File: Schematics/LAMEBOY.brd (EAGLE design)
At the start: 45.7 x 67.3 mm, 60 parts, among them IC1 PCF8574T, IC3 MCP73831, Q1 12MHz, U1 USD-SOCKETMICROSDEBAY, U2 USB

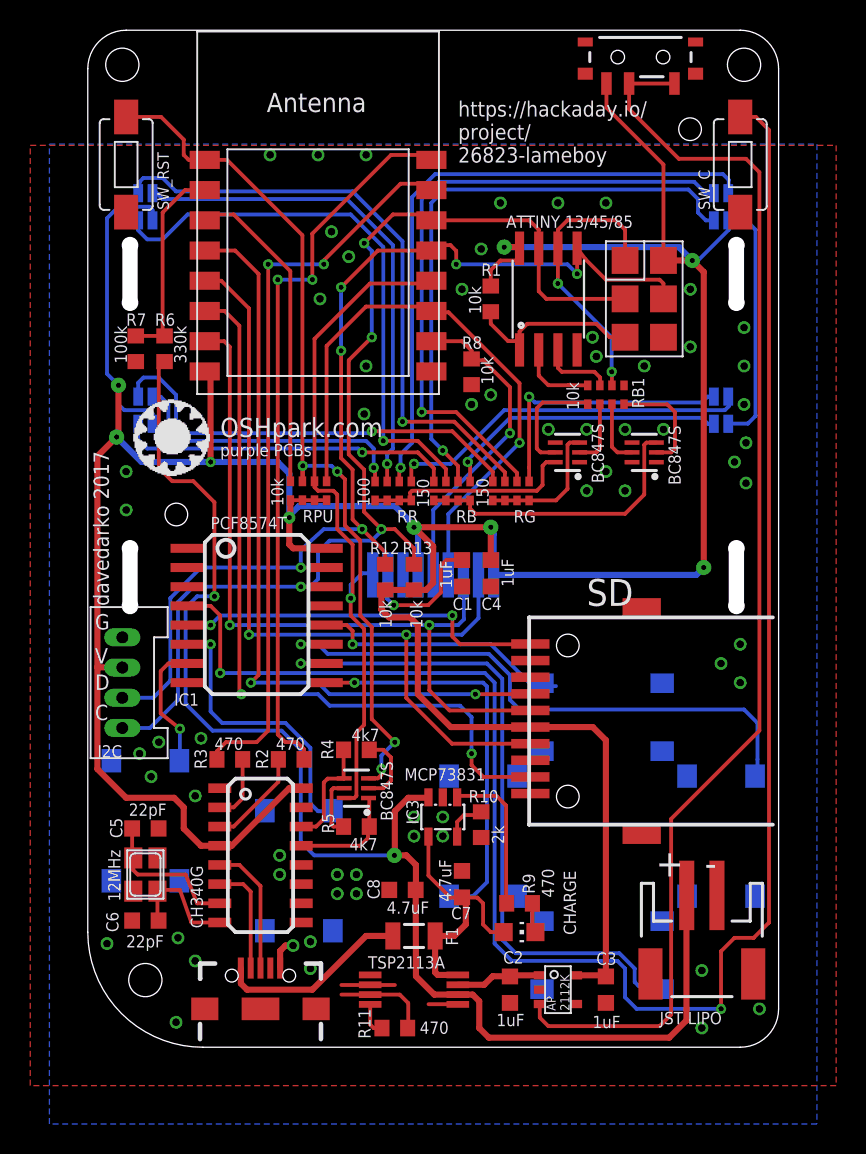
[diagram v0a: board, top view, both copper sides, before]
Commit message: bigger better resistor and crystal footprint
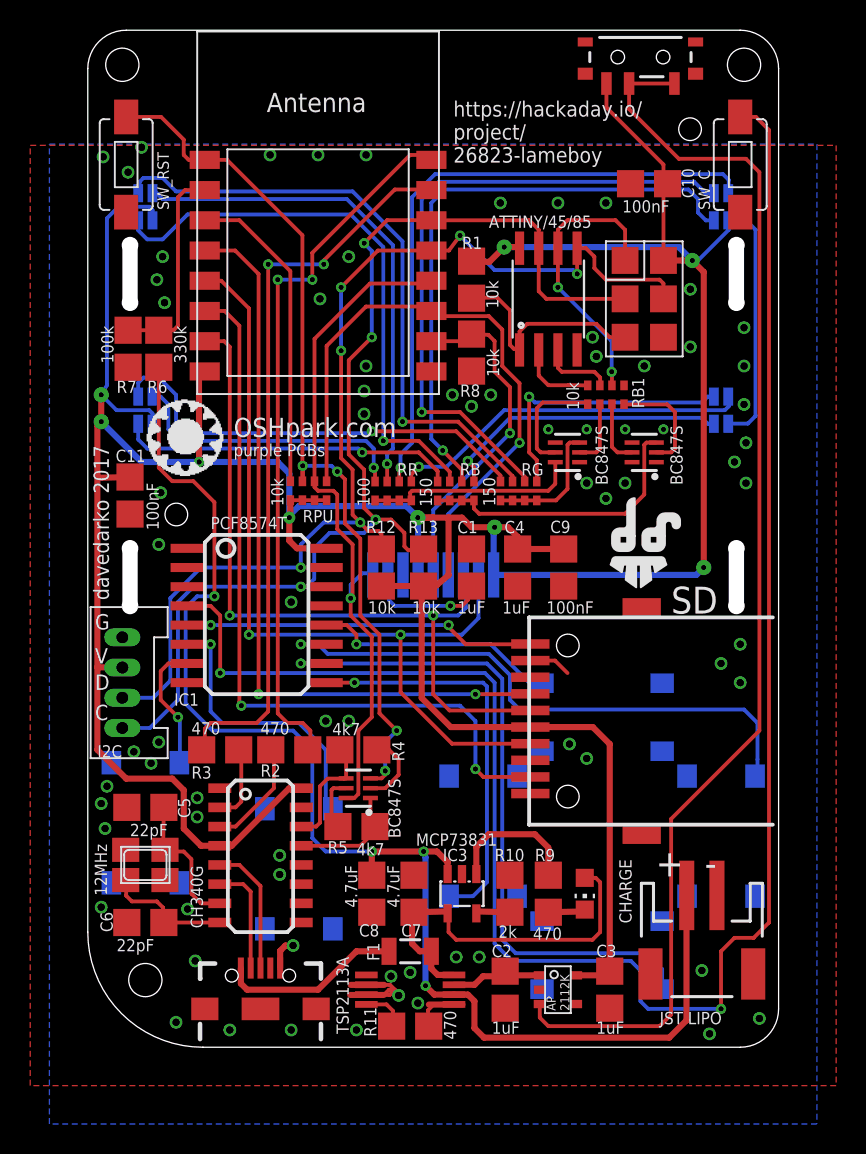
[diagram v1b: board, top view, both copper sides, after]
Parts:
- added C10, C11, C9: 100nF, rcl:ONEFITSALL
- added U$11: (no value), LOGOS:DAVEDARKO2_LOGO
- C1, C2, C3, C4, C5, C6, C7, C8: device rcl:C0603K -> rcl:ONEFITSALL
- Q1: device adafruit:NX3225 -> adafruit:NX3225_BIGGER
- R1, R10, R11, R12, R13, R2, R3, R4, R5, R6, R7, R8, R9: device rcl:R0603 -> rcl:ONEFITSALL
- U$8: device LOGOS:HACKADAY_LOGO -> LOGOS:DAVEDARKO_GOLD
- moved IC3 5.24 mm to (24.8, 10.2)
- moved CHARGE 5.01 mm to (32.9, 10.2), turned to 180 degrees
- moved R10 4.95 mm to (27.9, 10.2), turned to 270 degrees
- moved C7 3.24 mm to (21.6, 10.2)
- moved C8 2.05 mm to (18.8, 10.2), turned to 270 degrees
- moved R9 2.01 mm to (30.5, 10.2), turned to 90 degrees
- moved C4 1.82 mm to (28.4, 31.8)
- moved R1 1.80 mm to (25.4, 50.8)
- moved C5 1.40 mm to (3.81, 15.9), turned to 0 degrees
- moved R8 1.27 mm to (25.4, 46.0)
- moved U$8 1.05 mm to (34.0, 12.7), turned to 0 degrees
- moved F1 1.05 mm to (21.3, 6.35)
- moved R11 1.02 mm to (21.3, 1.40)
- moved R13 0.90 mm to (22.2, 31.8)
- moved R3 0.90 mm to (8.76, 19.7)
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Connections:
- net VREG_OUT renamed VREG_EN
- net ADC: now also R6.P$1, R7.P$2; no longer R6.1, R7.2
- net AVR_RST: now also R1.P$1; no longer R1.1
- net DTR: now also R5.P$1; no longer R5.1
- net GND: now also C1.P$2, C10.P$1, C11.P$1, C2.P$2, C3.P$2, C4.P$2, C5.P$1, C6.P$1, C7.P$1, C8.P$2, C9.P$1, R10.P$1, R11.P$1, R7.P$1, R8.P$2; no longer C1.2, C2.2, C3.2, C4.2, C5.1, C6.1, C7.1, C8.2, R10.1, R11.1, R7.1, R8.2
- net GPIO15: now also R8.P$1; no longer R8.1
- net N$12: now also R9.P$2; no longer R9.2
- net N$15: now also R9.P$1; no longer R9.1
- net N$17: now also C5.P$2; no longer C5.2
- net N$20: now also R11.P$2; no longer R11.2
- net N$21: now also R10.P$2; no longer R10.2
- net N$24: now also C6.P$2; no longer C6.2
- net N$25: now also R5.P$2; no longer R5.2
- net N$26: now also R2.P$2; no longer R2.2
- net N$27: now also R3.P$2; no longer R3.2
- net N$28: now also R4.P$2; no longer R4.2
- net N$8: now also C1.P$1; no longer C1.1
- net RTS: now also R4.P$1; no longer R4.1
- net RX_ESP: now also R3.P$1; no longer R3.1
- net SCL: now also R13.P$2; no longer R13.2
- net SDA: now also R12.P$2; no longer R12.2
- net TX_ESP: now also R2.P$1; no longer R2.1
- net VBAT: now also C8.P$1, R6.P$2; no longer C8.1, R6.2
- net VBUS: now also C7.P$2; no longer C7.2
- net VCC: now also C10.P$2, C11.P$2, C3.P$1, C4.P$1, C9.P$2, R1.P$2, R12.P$1, R13.P$1; no longer C3.1, C4.1, R1.2, R12.1, R13.1
- net VREG_IN: now also C2.P$1; no longer C2.1
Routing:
- net VBUS: track 18.2 -> 24.9 mm
- net VCC: track 254.7 -> 261.0 mm
- net GND: track 14.3 -> 17.8 mm, vias 63 -> 75
- net AVR_RST: track 12.4 -> 14.7 mm
- net BTN_UP: track 17.9 -> 16.3 mm
- net GPIO2: track 39.9 -> 41.3 mm
- net SD_IN: track 24.6 -> 23.3 mm
- net VREG_IN: track 5.70 -> 6.76 mm
- net DTR: track 7.34 -> 8.37 mm
- net GPIO15: track 21.7 -> 22.7 mm
- net TX_ESP: track 48.6 -> 47.6 mm
- net RX_ESP: track 48.9 -> 49.9 mm
- net N$20: track 2.21 -> 3.17 mm
- net N$12: track 10.1 -> 9.11 mm
- net N$21: track 3.13 -> 2.28 mm
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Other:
- board text added: "ATTINY/45/85"
- board text removed: "ATTINY 13/45/85"

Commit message: no idea. there's stuff changed so I push.
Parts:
- added U$12: (no value), LOGOS:HACKADAY_LOGO
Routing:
- net GND: vias 75 -> 76
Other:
- board text added: "*OR THE DISPLAY WON'T FIT"
- board text added: "ORDER 0.8MM BOARDS*"
- board text added: "Put the ESP8266 module here - it has all the WIFI"
- board text added: "This knows all the buttons"
- board text added: "This will come in handy one day. Please help."
- board text added: "USB serial converter"

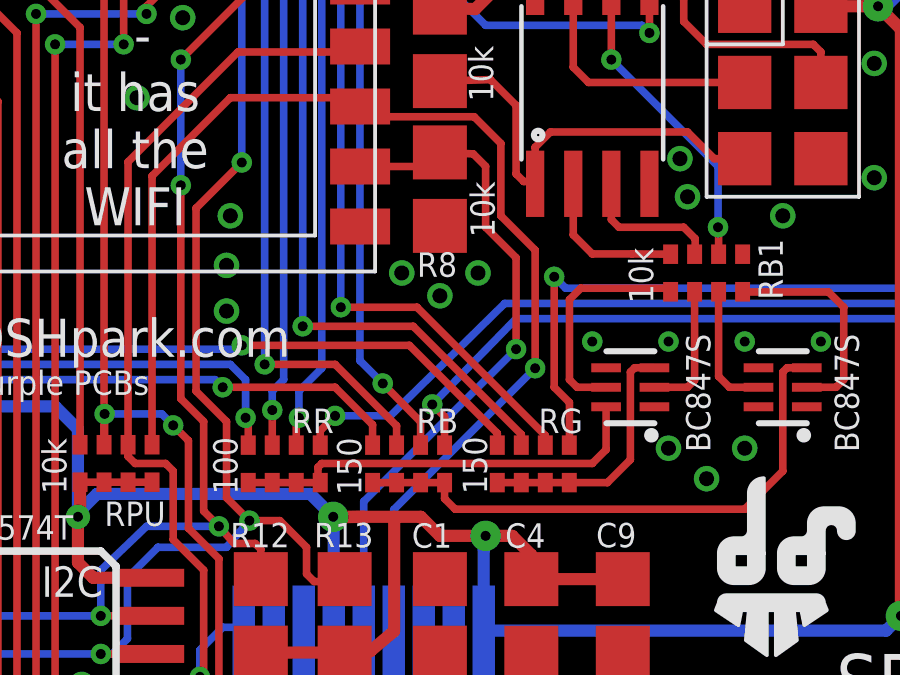
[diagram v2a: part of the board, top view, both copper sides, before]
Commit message: corrected rgb layout
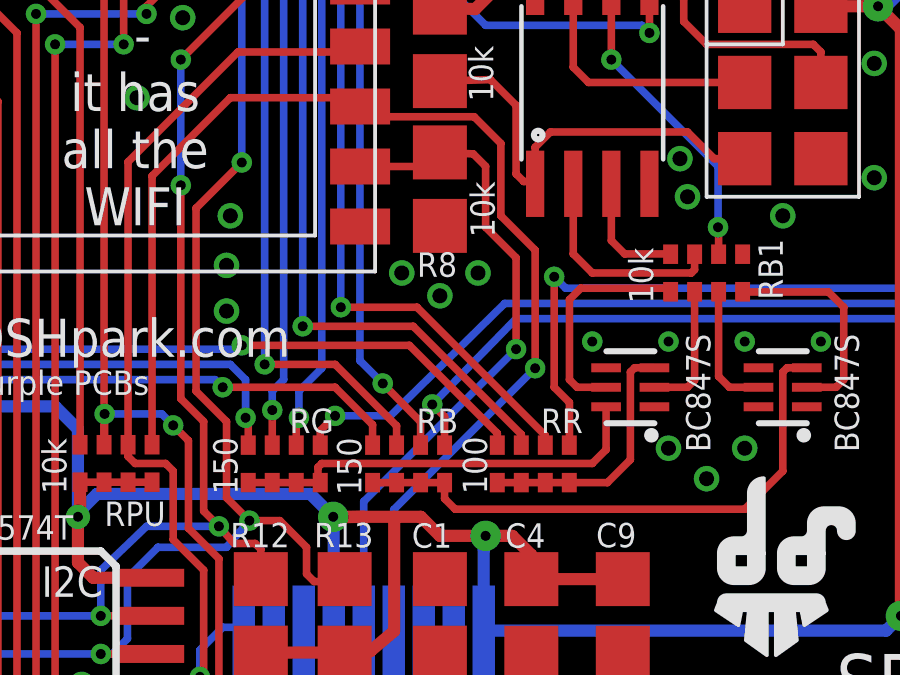
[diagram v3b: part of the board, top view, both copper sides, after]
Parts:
- moved RG 8.30 mm to (20.2, 36.8)
- moved RR 8.30 mm to (28.5, 36.8)
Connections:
- net N$1 renamed BLUE_LED
- removed net N$2: LED4.3, RR.4
- removed net N$3: LED4.2, RG.4
- new net GREEN_LED: LED4.3, RG.4
- new net RED_LED: LED4.2, RR.4
- net C_GRN: now also RB1.7; no longer RB1.8
- net C_RED: now also RB1.8; no longer RB1.7
- net GRN: now also U$6.6; no longer U$6.3
- net L2_R: now also RG.1; no longer RR.1
- net L4_G: now also RR.1; no longer RG.1
- net N$10: now also RR.2; no longer RG.2
- net N$5: now also RG.3; no longer RR.3
- net N$6: now also RR.3; no longer RG.3
- net N$9: now also RG.2; no longer RR.2
- net RED: now also U$6.3; no longer U$6.6
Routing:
- net RED_LED: track 0.00 -> 29.3 mm, vias 0 -> 1
- net N$3: track 29.3 -> 0.00 mm, vias 1 -> 0
- net N$2: track 19.2 -> 0.00 mm, vias 1 -> 0
- net GREEN_LED: track 0.00 -> 19.2 mm, vias 0 -> 1
- net RED: track 14.2 -> 8.53 mm
- net GRN: track 8.53 -> 14.2 mm
- net C_GRN: track 5.21 -> 7.21 mm
- net C_RED: track 4.78 -> 4.06 mm
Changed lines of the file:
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@@
 <layer number="20" name="Dimension" color="15" fill="1" visible="yes" active="yes"/>
 <layer number="21" name="tPlace" color="7" fill="1" visible="yes" active="yes"/>
-<layer number="22" name="bPlace" color="7" fill="1" visible="no" active="yes"/>
+<layer number="22" name="bPlace" color="7" fill="1" visible="yes" active="yes"/>
 <layer number="23" name="tOrigins" color="15" fill="1" visible="yes" active="yes"/>
-<layer number="24" name="bOrigins" color="15" fill="1" visible="no" active="yes"/>
+<layer number="24" name="bOrigins" color="15" fill="1" visible="yes" active="yes"/>
 <layer number="25" name="tNames" color="7" fill="1" visible="yes" active="yes"/>
-<layer number="26" name="bNames" color="7" fill="1" visible="no" active="yes"/>
-<layer number="27" name="tValues" color="7" fill="1" visible="no" active="yes"/>
-<layer number="28" name="bValues" color="7" fill="1" visible="no" active="yes"/>
+<layer number="26" name="bNames" color="7" fill="1" visible="yes" active="yes"/>
+<layer number="27" name="tValues" color="7" fill="1" visible="yes" active="yes"/>
+<layer number="28" name="bValues" color="7" fill="1" visible="yes" active="yes"/>
 <layer number="29" name="tStop" color="7" fill="3" visible="no" active="yes"/>
 <layer number="30" name="bStop" color="7" fill="6" visible="no" active="yes"/>
@@
 <attribute name="VALUE" x="22.7825" y="35.7785" size="0.8128" layer="25" ratio="12" rot="R90"/>
 </element>
-<element name="RR" library="resistor-dil" package="0603-ARC" value="100" x="20.212" y="36.816" smashed="yes" rot="R180">
+<element name="RG" library="resistor-dil" package="0603-ARC" value="150" x="20.212" y="36.816" smashed="yes" rot="R180">
 <attribute name="OC_FARNELL" value="unknown" x="20.212" y="36.816" size="1.778" layer="27" rot="R180" display="off"/>
 <attribute name="MPN" value="" x="20.212" y="36.816" size="1.778" layer="27" rot="R180" display="off"/>
@@
 <attribute name="VALUE" x="18.655" y="35.795" size="0.8128" layer="25" ratio="12" rot="R90"/>
 </element>
-<element name="RG" library="resistor-dil" package="0603-ARC" value="150" x="28.514" y="36.816" smashed="yes" rot="R180">
+<element name="RR" library="resistor-dil" package="0603-ARC" value="100" x="28.514" y="36.816" smashed="yes" rot="R180">
 <attribute name="OC_FARNELL" value="unknown" x="28.514" y="36.816" size="1.778" layer="27" rot="R180" display="off"/>
 <attribute name="MPN" value="" x="28.514" y="36.816" size="1.778" layer="27" rot="R180" display="off"/>
@@
 <wire x1="29.29" y1="20.09" x2="24.106" y2="20.09" width="0.254" layer="1"/>
 </signal>
-<signal name="N$1">
+<signal name="BLUE_LED">
 <contactref element="RB" pad="4"/>
 <contactref element="LED4" pad="1"/>
@@
 <wire x1="17.907" y1="39.624" x2="18.161" y2="39.37" width="0.254" layer="16"/>
 </signal>
-<signal name="N$2">
-<contactref element="RR" pad="4"/>
+<signal name="GREEN_LED">
+<contactref element="RG" pad="4"/>
 <contactref element="LED4" pad="3"/>
 <wire x1="19.012" y1="37.441" x2="19.012" y2="38.265" width="0.254" layer="1"/>
@@
 <wire x1="18.923" y1="39.624" x2="18.923" y2="38.354" width="0.254" layer="16"/>
 </signal>
-<signal name="N$3">
-<contactref element="RG" pad="4"/>
+<signal name="RED_LED">
+<contactref element="RR" pad="4"/>
 <contactref element="LED4" pad="2"/>
 <wire x1="27.314" y1="37.441" x2="27.314" y2="37.837" width="0.254" layer="1"/>
@@
 </signal>
 <signal name="N$5">
-<contactref element="RR" pad="3"/>
+<contactref element="RG" pad="3"/>
 <contactref element="LED3" pad="3"/>
 <wire x1="19.812" y1="37.441" x2="19.812" y2="38.608" width="0.254" layer="1"/>
@@
 </signal>
 <signal name="N$6">
-<contactref element="RG" pad="3"/>
+<contactref element="RR" pad="3"/>
 <contactref element="LED3" pad="2"/>
 <wire x1="28.114" y1="37.441" x2="28.114" y2="37.799" width="0.254" layer="1"/>
@@
 </signal>
 <signal name="N$9">
-<contactref element="RR" pad="2"/>
+<contactref element="RG" pad="2"/>
 <contactref element="LED2" pad="3"/>
 <wire x1="20.612" y1="37.441" x2="20.612" y2="38.189" width="0.254" layer="1"/>
@@
 </signal>
 <signal name="N$10">
-<contactref element="RG" pad="2"/>
+<contactref element="RR" pad="2"/>
 <contactref element="LED2" pad="2"/>
 <wire x1="41.43591875" y1="56.5252" x2="40.8838" y2="56.5252" width="0.254" layer="16"/>
@@
 </signal>
 <signal name="L2_R">
-<contactref element="RR" pad="1"/>
+<contactref element="RG" pad="1"/>
 <contactref element="LED1" pad="3"/>
 <wire x1="21.412" y1="37.441" x2="21.412" y2="37.922" width="0.254" layer="1"/>
@@
 </signal>
 <signal name="L4_G">
-<contactref element="RG" pad="1"/>
+<contactref element="RR" pad="1"/>
 <contactref element="LED1" pad="2"/>
 <via x="29.21" y="43.053" extent="1-16" drill="0.3302" diameter="0.635"/>
@@
 <signal name="C_GRN">
 <contactref element="U$2" pad="2"/>
-<contactref element="RB1" pad="8"/>
-<wire x1="29.845" y1="46.1518" x2="29.845" y2="44.45" width="0.254" layer="1"/>
-<wire x1="29.845" y1="44.45" x2="30.48" y2="43.815" width="0.254" layer="1"/>
-<wire x1="30.48" y1="43.815" x2="31.81" y2="43.815" width="0.254" layer="1"/>
-<wire x1="31.81" y1="43.815" x2="33.09" y2="43.805" width="0.254" layer="1"/>
+<wire x1="29.845" y1="46.1518" x2="29.845" y2="43.815" width="0.254" layer="1"/>
+<contactref element="RB1" pad="7"/>
+<wire x1="29.845" y1="43.815" x2="30.48" y2="43.18" width="0.254" layer="1"/>
+<wire x1="30.48" y1="43.18" x2="33.782" y2="43.18" width="0.254" layer="1"/>
+<wire x1="33.782" y1="43.18" x2="33.89" y2="43.288" width="0.254" layer="1"/>
+<wire x1="33.89" y1="43.805" x2="33.89" y2="43.288" width="0.254" layer="1"/>
 </signal>
 <signal name="MISO">
@@
 <signal name="C_RED">
 <contactref element="U$2" pad="3"/>
-<contactref element="RB1" pad="7"/>
-<wire x1="31.115" y1="46.1518" x2="31.115" y2="44.958" width="0.254" layer="1"/>
-<wire x1="31.115" y1="44.958" x2="31.369" y2="44.704" width="0.254" layer="1"/>
-<wire x1="31.369" y1="44.704" x2="33.528" y2="44.704" width="0.254" layer="1"/>
-<wire x1="33.528" y1="44.704" x2="33.909" y2="44.323" width="0.254" layer="1"/>
-<wire x1="33.909" y1="44.323" x2="33.909" y2="43.824" width="0.254" layer="1"/>
-<wire x1="33.909" y1="43.824" x2="33.89" y2="43.805" width="0.254" layer="1"/>
+<contactref element="RB1" pad="8"/>
+<wire x1="31.115" y1="46.1518" x2="31.115" y2="44.2595" width="0.254" layer="1"/>
+<wire x1="31.115" y1="44.2595" x2="31.5595" y2="43.815" width="0.254" layer="1"/>
+<wire x1="31.5595" y1="43.815" x2="33.08" y2="43.815" width="0.254" layer="1"/>
+<wire x1="33.08" y1="43.815" x2="33.09" y2="43.805" width="0.254" layer="1"/>
 </signal>
 <signal name="DP">
@@
 <wire x1="35.5" y1="42.545" x2="35.49" y2="42.555" width="0.254" layer="1"/>
 </signal>
-<signal name="GRN">
-<contactref element="RG" pad="8"/>
-<contactref element="RG" pad="7"/>
-<contactref element="RG" pad="6"/>
-<contactref element="RG" pad="5"/>
+<signal name="RED">
+<contactref element="RR" pad="8"/>
+<contactref element="RR" pad="7"/>
+<contactref element="RR" pad="6"/>
+<contactref element="RR" pad="5"/>
 <wire x1="27.314" y1="36.191" x2="28.114" y2="36.191" width="0.254" layer="1"/>
 <wire x1="28.114" y1="36.191" x2="28.914" y2="36.191" width="0.254" layer="1"/>
@@
 <wire x1="30.984" y1="36.191" x2="31.75" y2="36.957" width="0.254" layer="1"/>
 </signal>
-<signal name="RED">
-<contactref element="RR" pad="8"/>
-<contactref element="RR" pad="7"/>
-<contactref element="RR" pad="6"/>
-<contactref element="RR" pad="5"/>
+<signal name="GRN">
+<contactref element="RG" pad="8"/>
+<contactref element="RG" pad="7"/>
+<contactref element="RG" pad="6"/>
+<contactref element="RG" pad="5"/>
 <wire x1="19.012" y1="36.191" x2="19.812" y2="36.191" width="0.254" layer="1"/>
 <wire x1="19.812" y1="36.191" x2="20.612" y2="36.191" width="0.254" layer="1"/>
